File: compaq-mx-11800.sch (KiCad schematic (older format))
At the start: 238 parts

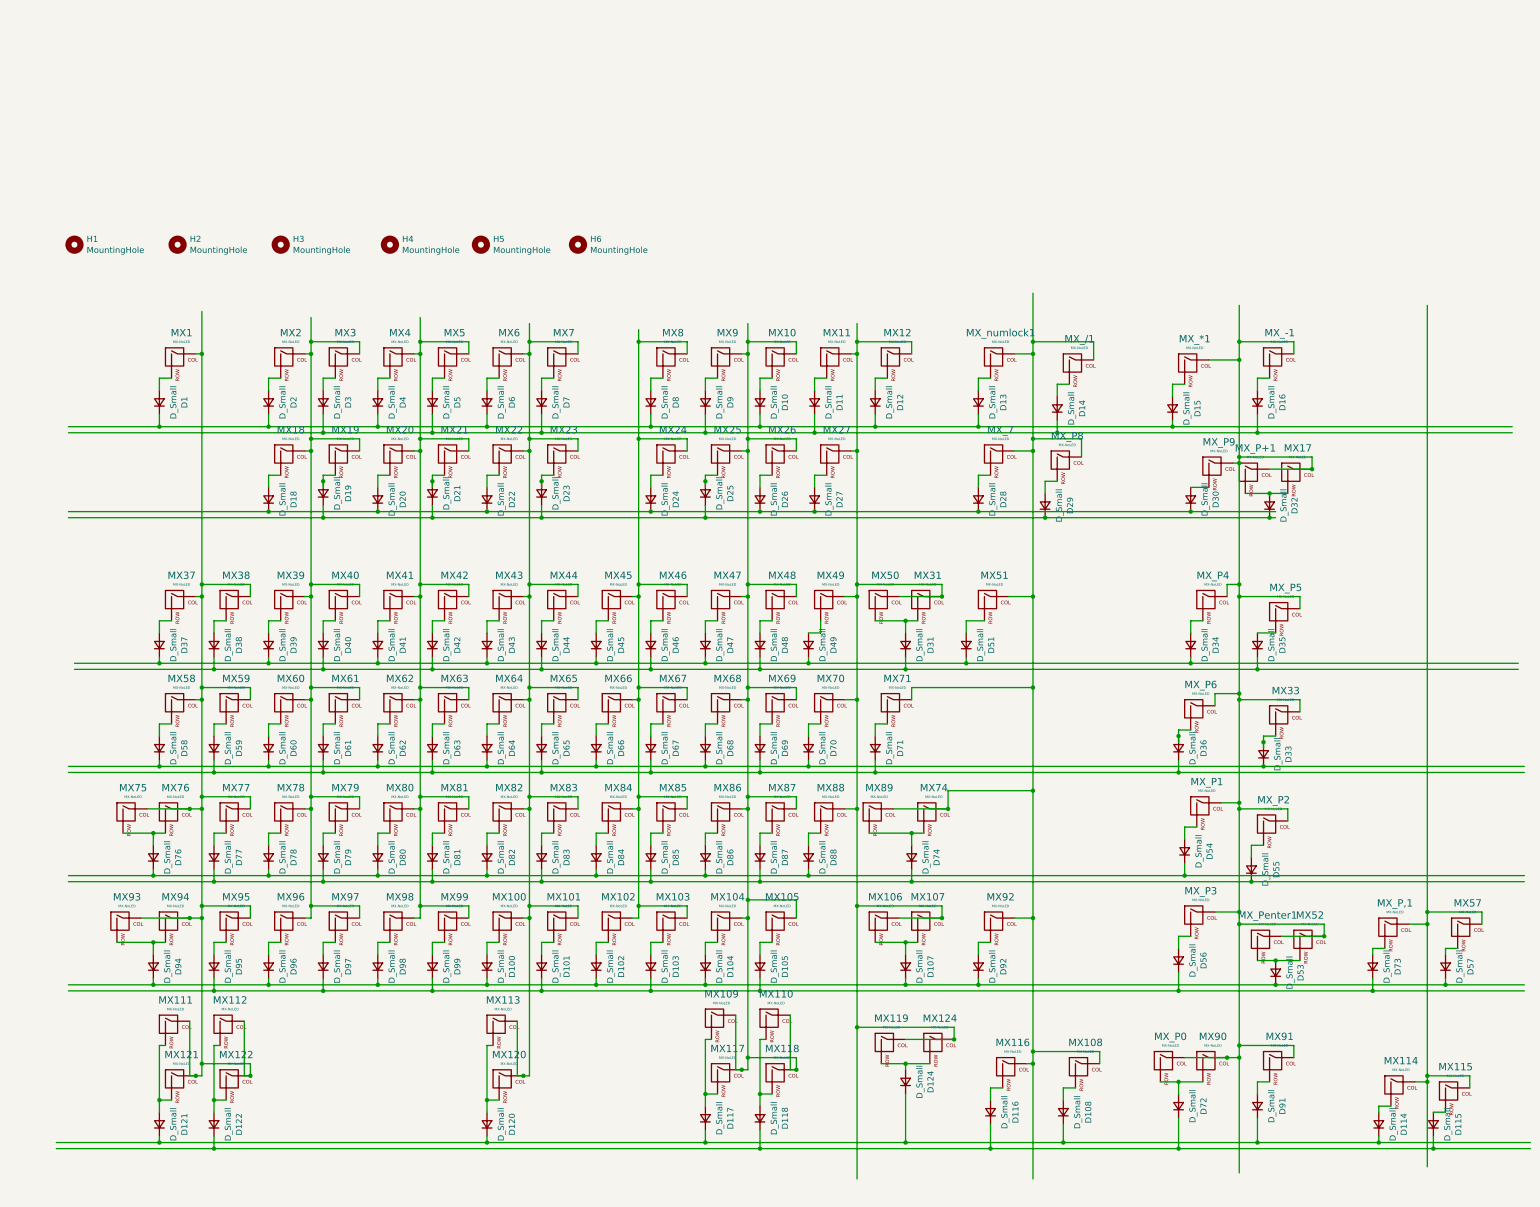
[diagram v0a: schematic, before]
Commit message: connect rows to output pins
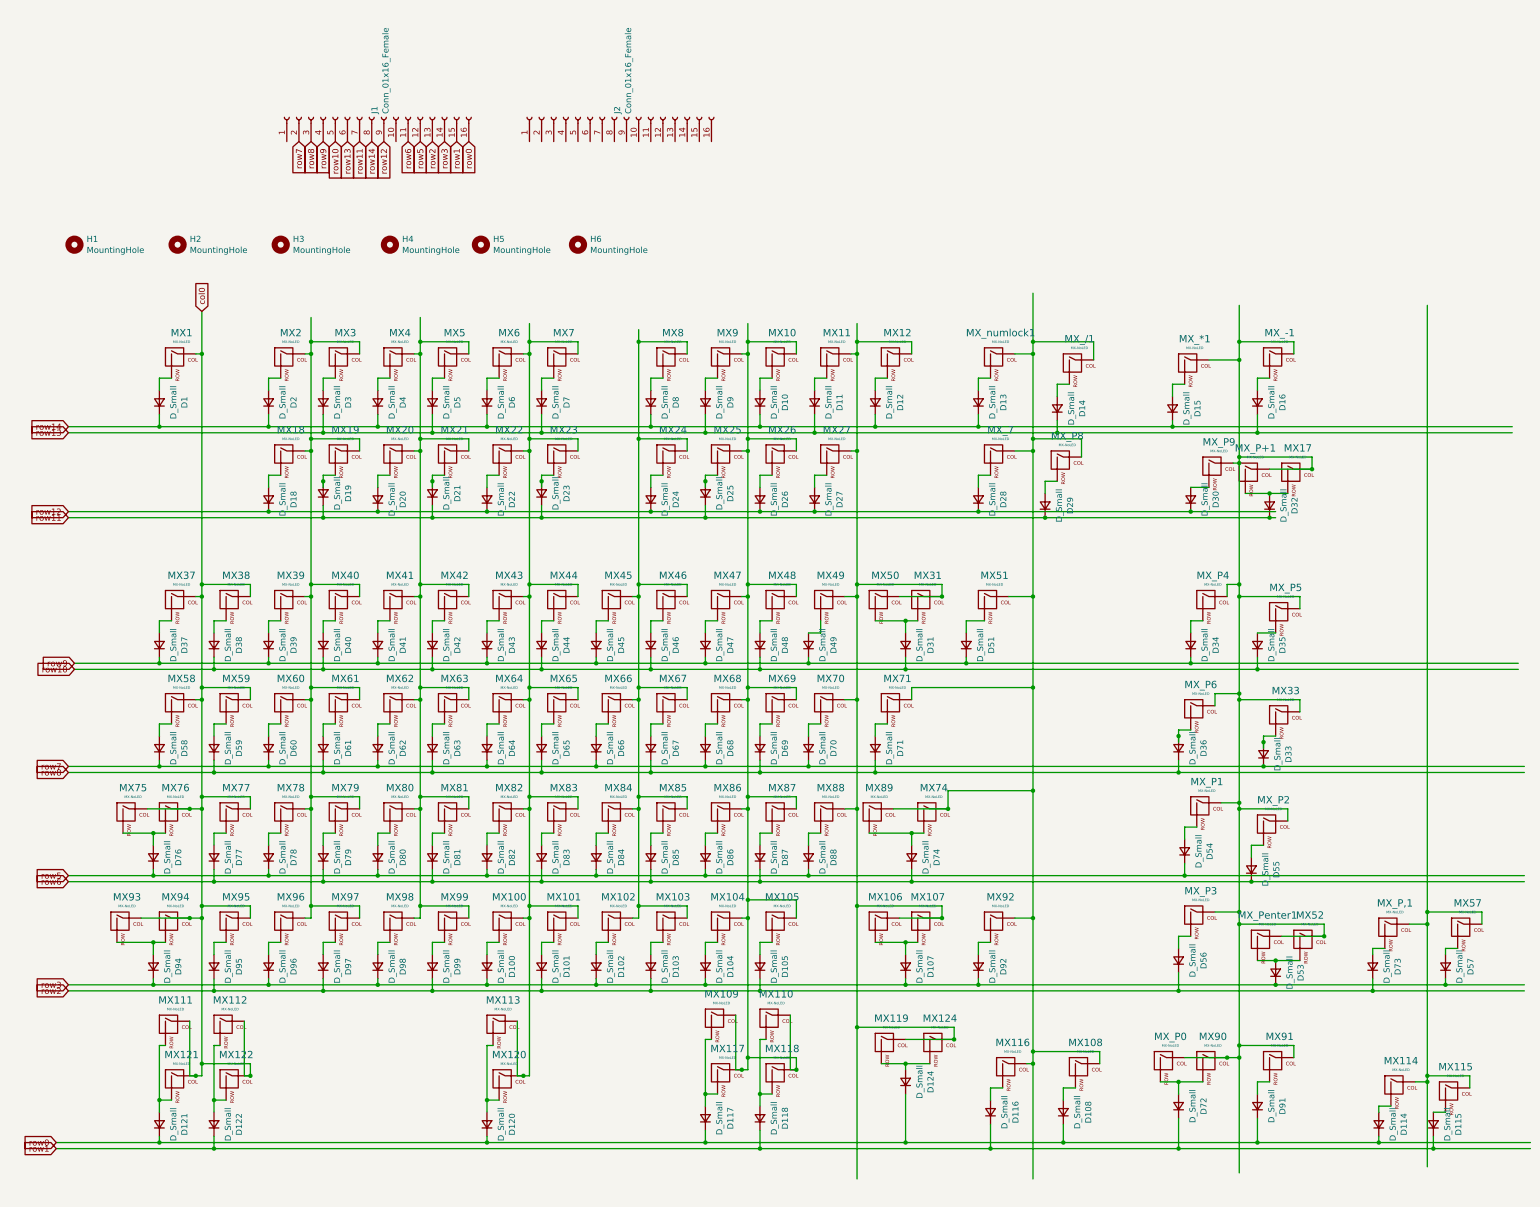
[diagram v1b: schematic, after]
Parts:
- added J1, J2: Conn_01x16_Female, Connector_PinHeader_2.54mm:PinHeader_1x16_P2.54mm_Vertical, symbol Connector:Conn_01x16_Female
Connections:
- net labels added: col0, row0, row1, row10, row11, row12, row13, row14, row2, row3, row5, row6, row7, row8, row9
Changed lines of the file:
@@
 Wire Wire Line
 	17800 13850 17800 14800
+$Comp
+L Connector:Conn_01x16_Female J1
+U 1 1 61E186A1
+P 10650 6100
+F 0 "J1" H 10678 6076 50  0000 L CNN
+F 1 "Conn_01x16_Female" H 10678 5985 50  0000 L CNN
+F 2 "Connector_PinHeader_2.54mm:PinHeader_1x16_P2.54mm_Vertical" H 10650 6100 50  0001 C CNN
+F 3 "~" H 10650 6100 50  0001 C CNN
+	1    10650 6100
+	0    -1   -1   0
+$EndComp
+$Comp
+L Connector:Conn_01x16_Female J2
+U 1 1 61F6C6A5
+P 12650 6100
+F 0 "J2" H 12678 6076 50  0000 L CNN
+F 1 "Conn_01x16_Female" H 12678 5985 50  0000 L CNN
+F 2 "Connector_PinHeader_2.54mm:PinHeader_1x16_P2.54mm_Vertical" H 12650 6100 50  0001 C CNN
+F 3 "~" H 12650 6100 50  0001 C CNN
+	1    12650 6100
+	0    -1   -1   0
+$EndComp
+Text GLabel 9250 7700 1    50   Input ~ 0
+col0
+Text GLabel 11450 6300 3    50   Input ~ 0
+row0
+Text GLabel 8050 14550 0    50   Input ~ 0
+row0
+Text GLabel 8050 14600 0    50   Input ~ 0
+row1
+Text GLabel 11350 6300 3    50   Input ~ 0
+row1
+Text GLabel 8150 13250 0    50   Input ~ 0
+row3
+Text GLabel 8150 13300 0    50   Input ~ 0
+row2
+Text GLabel 11250 6300 3    50   Input ~ 0
+row3
+Text GLabel 11150 6300 3    50   Input ~ 0
+row2
+Text GLabel 8150 12350 0    50   Input ~ 0
+row5
+Text GLabel 8150 12400 0    50   Input ~ 0
+row6
+Text GLabel 11050 6300 3    50   Input ~ 0
+row5
+Text GLabel 10950 6300 3    50   Input ~ 0
+row6
+Text GLabel 8150 11450 0    50   Input ~ 0
+row7
+Text GLabel 10050 6300 3    50   Input ~ 0
+row7
+Text GLabel 8150 11500 0    50   Input ~ 0
+row8
+Text GLabel 10150 6300 3    50   Input ~ 0
+row8
+Text GLabel 10250 6300 3    50   Input ~ 0
+row9
+Text GLabel 10350 6300 3    50   Input ~ 0
+row10
+Text GLabel 8200 10650 0    50   Input ~ 0
+row10
+Text GLabel 8200 10600 0    50   Input ~ 0
+row9
+Text GLabel 8150 9400 0    50   Input ~ 0
+row11
+Text GLabel 8150 9350 0    50   Input ~ 0
+row12
+Text GLabel 8150 8700 0    50   Input ~ 0
+row13
+Text GLabel 8150 8650 0    50   Input ~ 0
+row14
+Text GLabel 10750 6300 3    50   Input ~ 0
+row12
+Text GLabel 10550 6300 3    50   Input ~ 0
+row11
+Text GLabel 10450 6300 3    50   Input ~ 0
+row13
+Text GLabel 10650 6300 3    50   Input ~ 0
+row14
 $EndSCHEMATC

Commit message: fix some traces and stabilizer holes
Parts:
- MX74: footprint MX_Only:MXOnly-ISO-ROTATED-ReversedStabilizers-NoLED -> MX_Only:MXOnly-ISO-ReversedStabilizers-NoLED
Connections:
- net labels added: col1, col2, col3, col4, col5, col6, col7, col8, col9
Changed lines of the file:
@@
 F 0 "MX74" H 15283 12073 60  0000 C CNN
 F 1 "MX-NoLED" H 15283 11999 20  0000 C CNN
-F 2 "MX_Only:MXOnly-ISO-ROTATED-ReversedStabilizers-NoLED" H 14625 11825 60  0001 C CNN
+F 2 "MX_Only:MXOnly-ISO-ReversedStabilizers-NoLED" H 14625 11825 60  0001 C CNN
 F 3 "" H 14625 11825 60  0001 C CNN
 	1    15250 11850
@@
 Text GLabel 10650 6300 3    50   Input ~ 0
 row14
+Text GLabel 12350 6300 3    50   Input ~ 0
+col0
+Text GLabel 10150 7750 1    50   Input ~ 0
+col1
+Text GLabel 11050 7750 1    50   Input ~ 0
+col2
+Text GLabel 11950 7800 1    50   Input ~ 0
+col3
+Text GLabel 12250 6300 3    50   Input ~ 0
+col1
+Text GLabel 12150 6300 3    50   Input ~ 0
+col2
+Text GLabel 12050 6300 3    50   Input ~ 0
+col3
+Text GLabel 12850 7850 1    50   Input ~ 0
+col4
+Text GLabel 13750 7800 1    50   Input ~ 0
+col5
+Text GLabel 12450 6300 3    50   Input ~ 0
+col4
+Text GLabel 12550 6300 3    50   Input ~ 0
+col5
+Text GLabel 14650 7800 1    50   Input ~ 0
+col6
+Text GLabel 16100 7550 1    50   Input ~ 0
+col7
+Text GLabel 12650 6300 3    50   Input ~ 0
+col6
+Text GLabel 12750 6300 3    50   Input ~ 0
+col7
+Text GLabel 17800 7650 1    50   Input ~ 0
+col8
+Text GLabel 19350 7650 1    50   Input ~ 0
+col9
+Text GLabel 12850 6300 3    50   Input ~ 0
+col8
+Text GLabel 12950 6300 3    50   Input ~ 0
+col9
 $EndSCHEMATC

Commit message: reorder col and row pins
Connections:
- net labels added: row4
- net labels removed: row14
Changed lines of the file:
@@
 Wire Wire Line
 	8150 12350 8850 12350
-Wire Wire Line
-	8150 11450 8900 11450
 Connection ~ 15050 10650
 Wire Wire Line
@@
 	9800 8550 9800 8650
 Wire Wire Line
-	8900 8650 9800 8650
-Connection ~ 8900 8650
-Wire Wire Line
-	8900 8550 8900 8650
-Wire Wire Line
 	8150 8700 10250 8700
-Wire Wire Line
-	8150 8650 8900 8650
 $Comp
 L Device:D_Small D51
@@
 	1    0    0    -1
 $EndComp
-$Comp
-L Device:D_Small D1
-U 1 1 61C19A04
-P 8900 8450
-F 0 "D1" H 8900 8243 50  0000 C CNN
-F 1 "D_Small" H 8900 8334 50  0000 C CNN
-F 2 "Keebio-Parts:Diode-dual" V 8900 8450 50  0001 C CNN
-F 3 "~" V 8900 8450 50  0001 C CNN
-	1    8900 8450
-	0    -1   -1   0
-$EndComp
 Wire Wire Line
 	9000 8250 8900 8250
@@
 	15450 13600 14650 13600
 Wire Wire Line
-	8050 14550 8900 14550
-Wire Wire Line
-	8050 14600 9350 14600
-Wire Wire Line
 	8900 14500 8900 14550
-Connection ~ 8900 14550
 Wire Wire Line
 	8900 14550 11600 14550
 Wire Wire Line
 	9350 14500 9350 14600
-Connection ~ 9350 14600
 Wire Wire Line
 	9350 14600 13850 14600
@@
 $EndComp
 Text GLabel 9250 7700 1    50   Input ~ 0
+col3
+Text GLabel 10150 7750 1    50   Input ~ 0
+col2
+Text GLabel 11050 7750 1    50   Input ~ 0
+col1
+Text GLabel 11950 7800 1    50   Input ~ 0
 col0
-Text GLabel 11450 6300 3    50   Input ~ 0
-row0
-Text GLabel 8050 14550 0    50   Input ~ 0
+Text GLabel 12850 7850 1    50   Input ~ 0
+col4
+Text GLabel 13750 7800 1    50   Input ~ 0
+col5
+Text GLabel 14650 7800 1    50   Input ~ 0
+col6
+Text GLabel 16100 7550 1    50   Input ~ 0
+col7
+Text GLabel 17800 7650 1    50   Input ~ 0
+col8
+Text GLabel 19350 7650 1    50   Input ~ 0
+col9
+Text GLabel 8150 12350 0    50   Input ~ 0
+row9
+Text GLabel 8150 12400 0    50   Input ~ 0
+row8
+Text GLabel 8150 11450 0    50   Input ~ 0
 row0
-Text GLabel 8050 14600 0    50   Input ~ 0
-row1
-Text GLabel 11350 6300 3    50   Input ~ 0
-row1
-Text GLabel 8150 13250 0    50   Input ~ 0
-row3
-Text GLabel 8150 13300 0    50   Input ~ 0
-row2
-Text GLabel 11250 6300 3    50   Input ~ 0
+Text GLabel 8200 10650 0    50   Input ~ 0
 row3
-Text GLabel 11150 6300 3    50   Input ~ 0
+Text GLabel 8200 10600 0    50   Input ~ 0
 row2
-Text GLabel 8150 12350 0    50   Input ~ 0
+Text GLabel 8150 9400 0    50   Input ~ 0
 row5
-Text GLabel 8150 12400 0    50   Input ~ 0
+Text GLabel 8150 8650 0    50   Input ~ 0
 row6
-Text GLabel 11050 6300 3    50   Input ~ 0
+Text GLabel 8150 13300 0    50   Input ~ 0
+row10
+Text GLabel 8150 13250 0    50   Input ~ 0
+row11
+Connection ~ 9350 14600
+Wire Wire Line
+	8050 14600 9350 14600
+Connection ~ 8900 14550
+Wire Wire Line
+	8050 14550 8900 14550
+Text GLabel 10550 6300 3    50   Input ~ 0
 row5
+Text GLabel 10350 6300 3    50   Input ~ 0
+row3
+Text GLabel 10050 6300 3    50   Input ~ 0
+row0
+Text GLabel 11050 6300 3    50   Input ~ 0
+row9
 Text GLabel 10950 6300 3    50   Input ~ 0
+row8
+Text GLabel 11250 6300 3    50   Input ~ 0
+row11
+Text GLabel 11150 6300 3    50   Input ~ 0
+row10
+Text GLabel 11350 6300 3    50   Input ~ 0
+row12
+Text GLabel 11450 6300 3    50   Input ~ 0
+row13
+Text GLabel 8150 8700 0    50   Input ~ 0
+row4
+Text GLabel 10650 6300 3    50   Input ~ 0
 row6
-Text GLabel 8150 11450 0    50   Input ~ 0
+Text GLabel 8150 9350 0    50   Input ~ 0
 row7
-Text GLabel 10050 6300 3    50   Input ~ 0
+Text GLabel 10750 6300 3    50   Input ~ 0
 row7
 Text GLabel 8150 11500 0    50   Input ~ 0
-row8
+row1
+Text GLabel 10450 6300 3    50   Input ~ 0
+row4
 Text GLabel 10150 6300 3    50   Input ~ 0
-row8
+row1
 Text GLabel 10250 6300 3    50   Input ~ 0
-row9
-Text GLabel 10350 6300 3    50   Input ~ 0
-row10
-Text GLabel 8200 10650 0    50   Input ~ 0
-row10
-Text GLabel 8200 10600 0    50   Input ~ 0
-row9
-Text GLabel 8150 9400 0    50   Input ~ 0
-row11
-Text GLabel 8150 9350 0    50   Input ~ 0
-row12
-Text GLabel 8150 8700 0    50   Input ~ 0
+row2
+Text GLabel 8050 14550 0    50   Input ~ 0
 row13
-Text GLabel 8150 8650 0    50   Input ~ 0
-row14
-Text GLabel 10750 6300 3    50   Input ~ 0
+Text GLabel 8050 14600 0    50   Input ~ 0
 row12
-Text GLabel 10550 6300 3    50   Input ~ 0
-row11
-Text GLabel 10450 6300 3    50   Input ~ 0
-row13
-Text GLabel 10650 6300 3    50   Input ~ 0
-row14
-Text GLabel 12350 6300 3    50   Input ~ 0
+Wire Wire Line
+	8150 11450 8900 11450
+$Comp
+L Device:D_Small D1
+U 1 1 61C19A04
+P 8900 8450
+F 0 "D1" H 8900 8243 50  0000 C CNN
+F 1 "D_Small" H 8900 8334 50  0000 C CNN
+F 2 "Keebio-Parts:Diode-dual" V 8900 8450 50  0001 C CNN
+F 3 "~" V 8900 8450 50  0001 C CNN
+	1    8900 8450
+	0    -1   -1   0
+$EndComp
+Wire Wire Line
+	8150 8650 8900 8650
+Wire Wire Line
+	8900 8650 9800 8650
+Connection ~ 8900 8650
+Wire Wire Line
+	8900 8550 8900 8650
+Text GLabel 12050 6300 3    50   Input ~ 0
 col0
-Text GLabel 10150 7750 1    50   Input ~ 0
+Text GLabel 12150 6300 3    50   Input ~ 0
 col1
-Text GLabel 11050 7750 1    50   Input ~ 0
-col2
-Text GLabel 11950 7800 1    50   Input ~ 0
-col3
 Text GLabel 12250 6300 3    50   Input ~ 0
-col1
-Text GLabel 12150 6300 3    50   Input ~ 0
 col2
-Text GLabel 12050 6300 3    50   Input ~ 0
+Text GLabel 12350 6300 3    50   Input ~ 0
 col3
-Text GLabel 12850 7850 1    50   Input ~ 0
-col4
-Text GLabel 13750 7800 1    50   Input ~ 0
-col5
 Text GLabel 12450 6300 3    50   Input ~ 0
 col4
 Text GLabel 12550 6300 3    50   Input ~ 0
 col5
-Text GLabel 14650 7800 1    50   Input ~ 0
-col6
-Text GLabel 16100 7550 1    50   Input ~ 0
-col7
 Text GLabel 12650 6300 3    50   Input ~ 0
 col6
 Text GLabel 12750 6300 3    50   Input ~ 0
 col7
-Text GLabel 17800 7650 1    50   Input ~ 0
-col8
-Text GLabel 19350 7650 1    50   Input ~ 0
-col9
 Text GLabel 12850 6300 3    50   Input ~ 0
 col8

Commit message: cleanup .sch
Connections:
- wire segments 754 -> 776
